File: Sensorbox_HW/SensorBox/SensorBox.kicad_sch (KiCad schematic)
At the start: 81 parts, among them U1 BME280, U11 PS1-O3-100, U12 DS3231M, U13 OPA197xD, U2 OPA197xD, U4 MC33063AD, U5 OPA197xD, U6 MAX31855EASA, U8 HPP845E131R5

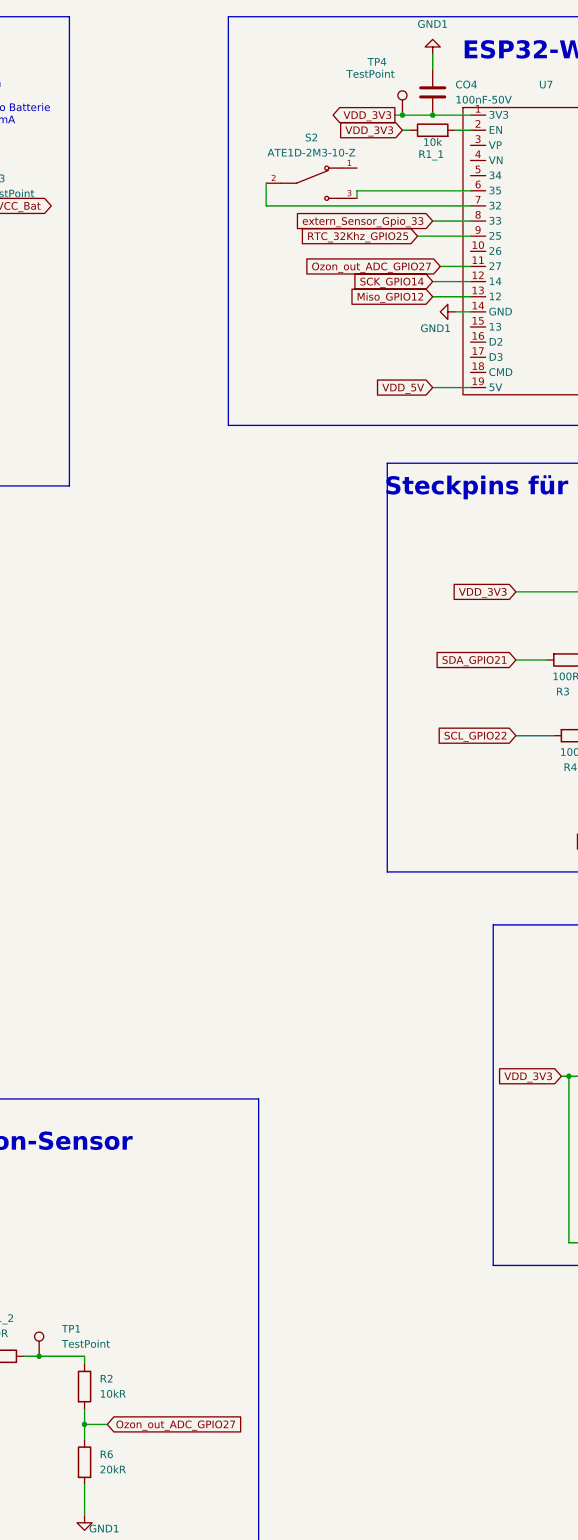
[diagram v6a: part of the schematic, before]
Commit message: Ozon Pin zum ESP geändert
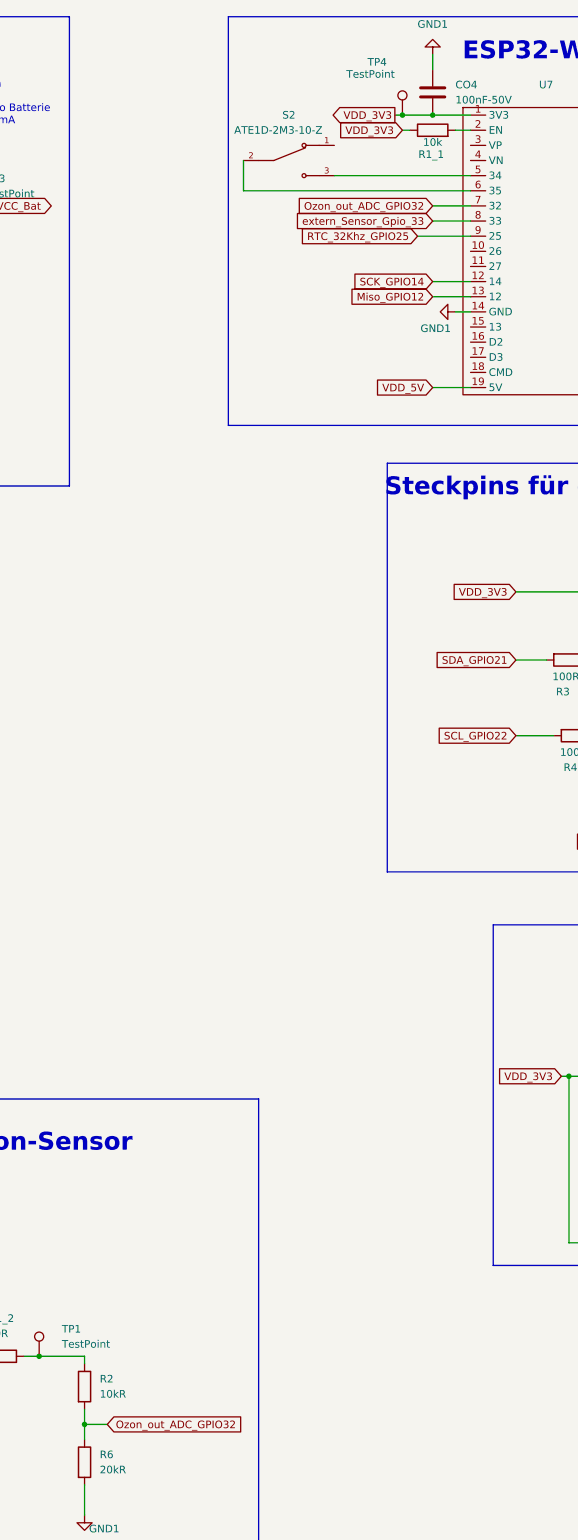
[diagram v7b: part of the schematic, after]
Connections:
- net at S2.2: now also U7.6 (35); no longer U7.7 (32)
- net at S2.3: now also U7.5 (34); no longer U7.6 (35)
- net Ozon_out_ADC_GPIO27 renamed Ozon_out_ADC_GPIO32
- net Ozon_out_ADC_GPIO32: now also U7.7 (32); no longer U7.11 (27)
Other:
- moved on the sheet: S2
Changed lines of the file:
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@@
 	(wire
 		(pts
-			(xy 222.25 40.64) (xy 222.25 44.45)
+			(xy 218.44 41.91) (xy 218.44 36.83)
 		)
 		(stroke
@@
 	(wire
 		(pts
+			(xy 218.44 41.91) (xy 256.54 41.91)
+		)
+		(stroke
+			(width 0)
+			(type default)
+		)
+	)
+	(wire
+		(pts
 			(xy 373.38 82.55) (xy 377.19 82.55)
 		)
@@
 	(wire
 		(pts
-			(xy 222.25 44.45) (xy 256.54 44.45)
-		)
-		(stroke
-			(width 0)
-			(type default)
-		)
-	)
-	(wire
-		(pts
 			(xy 191.77 248.92) (xy 195.58 248.92)
 		)
@@
 	(wire
 		(pts
+			(xy 256.54 39.37) (xy 233.68 39.37)
+		)
+		(stroke
+			(width 0)
+			(type default)
+		)
+	)
+	(wire
+		(pts
 			(xy 80.01 60.96) (xy 80.01 62.23)
 		)
@@
 	(wire
 		(pts
-			(xy 256.54 41.91) (xy 237.49 41.91)
-		)
-		(stroke
-			(width 0)
-			(type default)
-		)
-	)
-	(wire
-		(pts
 			(xy 171.45 237.49) (xy 171.45 259.08)
 		)
@@
 	(wire
 		(pts
-			(xy 251.46 54.61) (xy 256.54 54.61)
-		)
-		(stroke
-			(width 0)
-			(type default)
-		)
-	)
-	(wire
-		(pts
 			(xy 93.98 254) (xy 93.98 256.54)
 		)
@@
 	(wire
 		(pts
-			(xy 237.49 41.91) (xy 237.49 43.18)
+			(xy 370.84 104.14) (xy 386.08 104.14)
 		)
 		(stroke
@@
 	(wire
 		(pts
-			(xy 370.84 104.14) (xy 386.08 104.14)
+			(xy 78.74 52.07) (xy 80.01 52.07)
 		)
 		(stroke
@@
 	(wire
 		(pts
-			(xy 78.74 52.07) (xy 80.01 52.07)
+			(xy 36.83 173.99) (xy 36.83 176.53)
 		)
 		(stroke
@@
 	(wire
 		(pts
-			(xy 36.83 173.99) (xy 36.83 176.53)
+			(xy 361.95 26.67) (xy 361.95 30.48)
 		)
 		(stroke
@@
 	(wire
 		(pts
-			(xy 361.95 26.67) (xy 361.95 30.48)
+			(xy 250.19 44.45) (xy 256.54 44.45)
 		)
 		(stroke
@@
 		)
 	)
-	(global_label "Ozon_out_ADC_GPIO27"
-		(shape input)
-		(at 251.46 54.61 180)
-		(fields_autoplaced yes)
-		(effects
-			(font
-				(size 1.27 1.27)
-			)
-			(justify right)
-		)
-		(property "Intersheetrefs" "${INTERSHEET_REFS}"
-			(at 227.3688 54.61 0)
-			(effects
-				(font
-					(size 1.27 1.27)
-				)
-				(justify right)
-				(hide yes)
-			)
-		)
-	)
 	(global_label "Miso_GPIO19"
 		(shape input)
@@
 		)
 	)
+	(global_label "Ozon_out_ADC_GPIO32"
+		(shape input)
+		(at 250.19 44.45 180)
+		(fields_autoplaced yes)
+		(effects
+			(font
+				(size 1.27 1.27)
+			)
+			(justify right)
+		)
+		(property "Intersheetrefs" "${INTERSHEET_REFS}"
+			(at 226.0988 44.45 0)
+			(effects
+				(font
+					(size 1.27 1.27)
+				)
+				(justify right)
+				(hide yes)
+			)
+		)
+	)
 	(global_label "VDD_3V3"
 		(shape input)
@@
 		)
 	)
-	(global_label "Ozon_out_ADC_GPIO27"
+	(global_label "Ozon_out_ADC_GPIO32"
 		(shape input)
 		(at 195.58 248.92 0)
@@
 	(symbol
 		(lib_id "Schalter_neu:ATE1D-2M3-10-Z")
-		(at 229.87 40.64 0)
+		(at 226.06 36.83 0)
 		(unit 1)
 		(exclude_from_sim no)
@@
 		(on_board yes)
 		(dnp no)
-		(fields_autoplaced yes)
 		(property "Reference" "S2"
-			(at 229.87 33.02 0)
+			(at 226.06 29.21 0)
 			(effects
 				(font
@@
 		)
 		(property "Value" "ATE1D-2M3-10-Z"
-			(at 229.87 35.56 0)
+			(at 224.282 31.75 0)
 			(effects
 				(font
@@
 		)
 		(property "Footprint" "Schalter_neu:SW_ATE1D-2M3-10-Z"
-			(at 229.87 40.64 0)
+			(at 226.06 36.83 0)
 			(effects
 				(font
@@
 		)
 		(property "Datasheet" ""
-			(at 229.87 40.64 0)
+			(at 226.06 36.83 0)
 			(effects
 				(font
@@
 		)
 		(property "Description" ""
-			(at 229.87 40.64 0)
+			(at 226.06 36.83 0)
 			(effects
 				(font
@@
 		)
 		(property "MF" ""
-			(at 229.87 40.64 0)
+			(at 226.06 36.83 0)
 			(effects
 				(font
@@
 		)
 		(property "MAXIMUM_PACKAGE_HEIGHT" ""
-			(at 229.87 40.64 0)
+			(at 226.06 36.83 0)
 			(effects
 				(font
@@
 		)
 		(property "Package" ""
-			(at 229.87 40.64 0)
+			(at 226.06 36.83 0)
 			(effects
 				(font
@@
 		)
 		(property "Price" ""
-			(at 229.87 40.64 0)
+			(at 226.06 36.83 0)
 			(effects
 				(font
@@
 		)
 		(property "Check_prices" ""
-			(at 229.87 40.64 0)
+			(at 226.06 36.83 0)
 			(effects
 				(font
@@
 		)
 		(property "STANDARD" ""
-			(at 229.87 40.64 0)
+			(at 226.06 36.83 0)
 			(effects
 				(font
@@
 		)
 		(property "PARTREV" ""
-			(at 229.87 40.64 0)
+			(at 226.06 36.83 0)
 			(effects
 				(font
@@
 		)
 		(property "SnapEDA_Link" ""
-			(at 229.87 40.64 0)
+			(at 226.06 36.83 0)
 			(effects
 				(font
@@
 		)
 		(property "MP" ""
-			(at 229.87 40.64 0)
+			(at 226.06 36.83 0)
 			(effects
 				(font
@@
 		)
 		(property "Description_1" ""
-			(at 229.87 40.64 0)
+			(at 226.06 36.83 0)
 			(effects
 				(font
@@
 		)
 		(property "Availability" ""
-			(at 229.87 40.64 0)
+			(at 226.06 36.83 0)
 			(effects
 				(font
@@
 		)
 		(property "MANUFACTURER" ""
-			(at 229.87 40.64 0)
+			(at 226.06 36.83 0)
 			(effects
 				(font

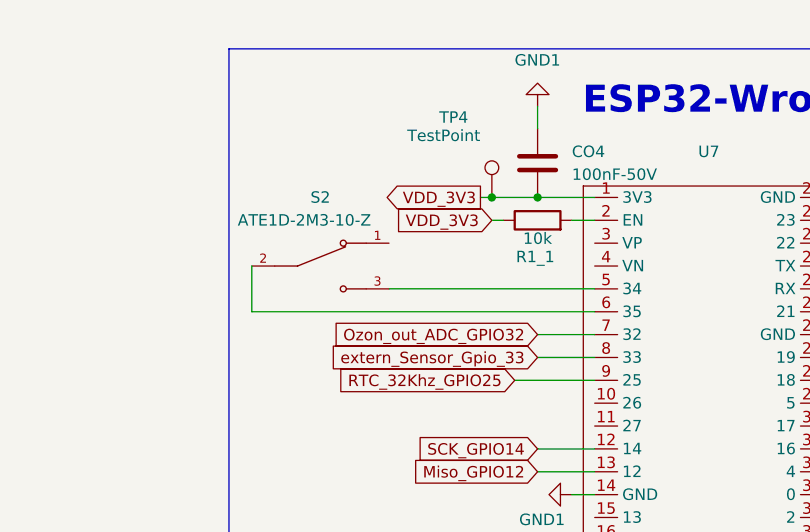
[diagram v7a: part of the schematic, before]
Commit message: Schalter zwischen GPIOS entfernt
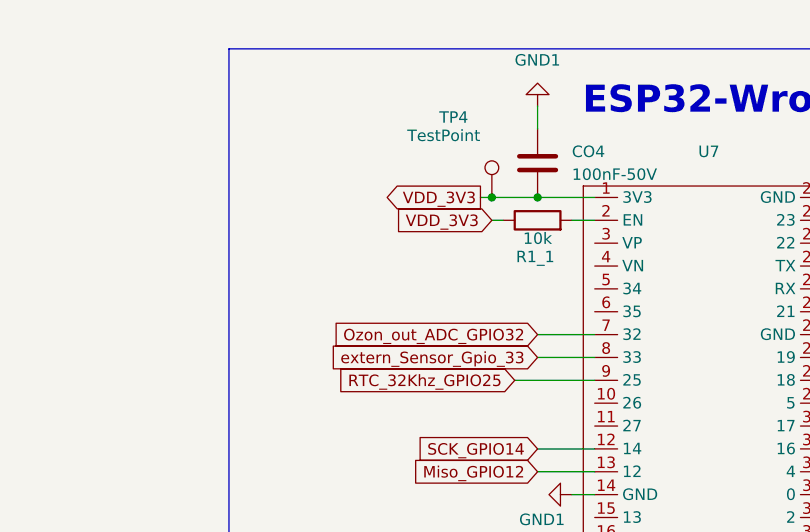
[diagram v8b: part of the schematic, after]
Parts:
- removed S2: ATE1D-2M3-10-Z, Schalter_neu:SW_ATE1D-2M3-10-Z, symbol Schalter_neu:ATE1D-2M3-10-Z
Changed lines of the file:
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@@
 	(wire
 		(pts
-			(xy 218.44 41.91) (xy 218.44 36.83)
-		)
-		(stroke
-			(width 0)
-			(type default)
-		)
-	)
-	(wire
-		(pts
 			(xy 271.78 190.5) (xy 273.05 190.5)
 		)
@@
 	(wire
 		(pts
-			(xy 218.44 41.91) (xy 256.54 41.91)
-		)
-		(stroke
-			(width 0)
-			(type default)
-		)
-	)
-	(wire
-		(pts
 			(xy 373.38 82.55) (xy 377.19 82.55)
 		)
@@
 	(wire
 		(pts
-			(xy 256.54 39.37) (xy 233.68 39.37)
-		)
-		(stroke
-			(width 0)
-			(type default)
-		)
-	)
-	(wire
-		(pts
 			(xy 80.01 60.96) (xy 80.01 62.23)
 		)
@@
 					(unit 1)
 				)
-			)
-		)
-	)
-	(symbol
-		(lib_id "Schalter_neu:ATE1D-2M3-10-Z")
-		(at 226.06 36.83 0)
-		(unit 1)
-		(exclude_from_sim no)
-		(in_bom yes)
-		(on_board yes)
-		(dnp no)
-		(property "Reference" "S2"
-			(at 226.06 29.21 0)
-			(effects
-				(font
-					(size 1.27 1.27)
-				)
-			)
-		)
-		(property "Value" "ATE1D-2M3-10-Z"
-			(at 224.282 31.75 0)
-			(effects
-				(font
-					(size 1.27 1.27)
-				)
-			)
-		)
-		(property "Footprint" "Schalter_neu:SW_ATE1D-2M3-10-Z"
-			(at 226.06 36.83 0)
-			(effects
-				(font
-					(size 1.27 1.27)
-				)
-				(justify bottom)
-				(hide yes)
-			)
-		)
-		(property "Datasheet" ""
-			(at 226.06 36.83 0)
-			(effects
-				(font
-					(size 1.27 1.27)
-				)
-				(hide yes)
-			)
-		)
-		(property "Description" ""
-			(at 226.06 36.83 0)
-			(effects
-				(font
-					(size 1.27 1.27)
-				)
-				(hide yes)
-			)
-		)
-		(property "MF" ""
-			(at 226.06 36.83 0)
-			(effects
-				(font
-					(size 1.27 1.27)
-				)
-				(justify bottom)
-				(hide yes)
-			)
-		)
-		(property "MAXIMUM_PACKAGE_HEIGHT" ""
-			(at 226.06 36.83 0)
-			(effects
-				(font
-					(size 1.27 1.27)
-				)
-				(justify bottom)
-				(hide yes)
-			)
-		)
-		(property "Package" ""
-			(at 226.06 36.83 0)
-			(effects
-				(font
-					(size 1.27 1.27)
-				)
-				(justify bottom)
-				(hide yes)
-			)
-		)
-		(property "Price" ""
-			(at 226.06 36.83 0)
-			(effects
-				(font
-					(size 1.27 1.27)
-				)
-				(justify bottom)
-				(hide yes)
-			)
-		)
-		(property "Check_prices" ""
-			(at 226.06 36.83 0)
-			(effects
-				(font
-					(size 1.27 1.27)
-				)
-				(justify bottom)
-				(hide yes)
-			)
-		)
-		(property "STANDARD" ""
-			(at 226.06 36.83 0)
-			(effects
-				(font
-					(size 1.27 1.27)
-				)
-				(justify bottom)
-				(hide yes)
-			)
-		)
-		(property "PARTREV" ""
-			(at 226.06 36.83 0)
-			(effects
-				(font
-					(size 1.27 1.27)
-				)
-				(justify bottom)
-				(hide yes)
-			)
-		)
-		(property "SnapEDA_Link" ""
-			(at 226.06 36.83 0)
-			(effects
-				(font
-					(size 1.27 1.27)
-				)
-				(justify bottom)
-				(hide yes)
-			)
-		)
-		(property "MP" ""
-			(at 226.06 36.83 0)
-			(effects
-				(font
-					(size 1.27 1.27)
-				)
-				(justify bottom)
-				(hide yes)
-			)
-		)
-		(property "Description_1" ""
-			(at 226.06 36.83 0)
-			(effects
-				(font
-					(size 1.27 1.27)
-				)
-				(justify bottom)
-				(hide yes)
-			)
-		)
-		(property "Availability" ""
-			(at 226.06 36.83 0)
-			(effects
-				(font
-					(size 1.27 1.27)
-				)
-				(justify bottom)
-				(hide yes)
-			)
-		)
-		(property "MANUFACTURER" ""
-			(at 226.06 36.83 0)
-			(effects
-				(font
-					(size 1.27 1.27)
-				)
-				(justify bottom)
-				(hide yes)
-			)
-		)
-		(pin "3"
-		)
-		(pin "1"
-		)
-		(pin "2"
-		)
-		(instances
-			(project "SensorBox"
-				(path "/7cbe8151-7294-42e6-9c4e-6ec8952d674f"
-					(reference "S2")
-					(unit 1)
-				)
